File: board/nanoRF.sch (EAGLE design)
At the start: 19 parts

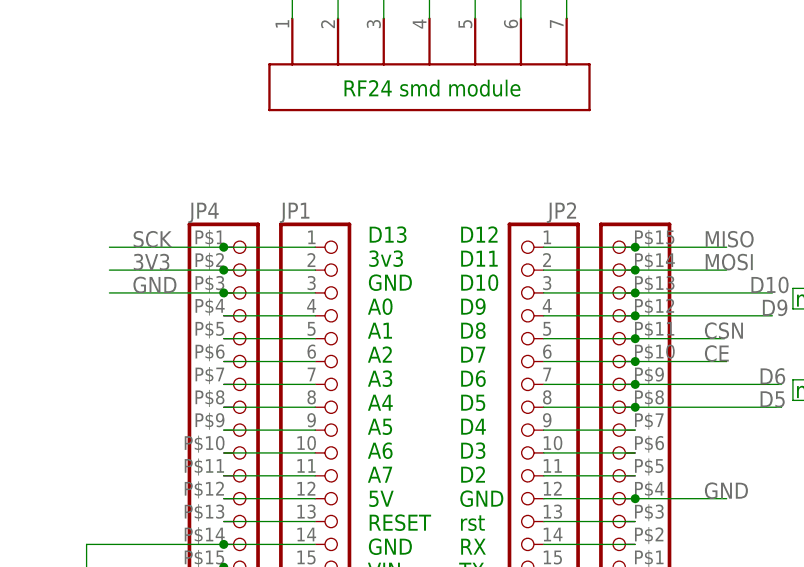
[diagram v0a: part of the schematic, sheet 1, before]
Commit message: changed prj name and files to nanoRF, starting fix for AREF pin
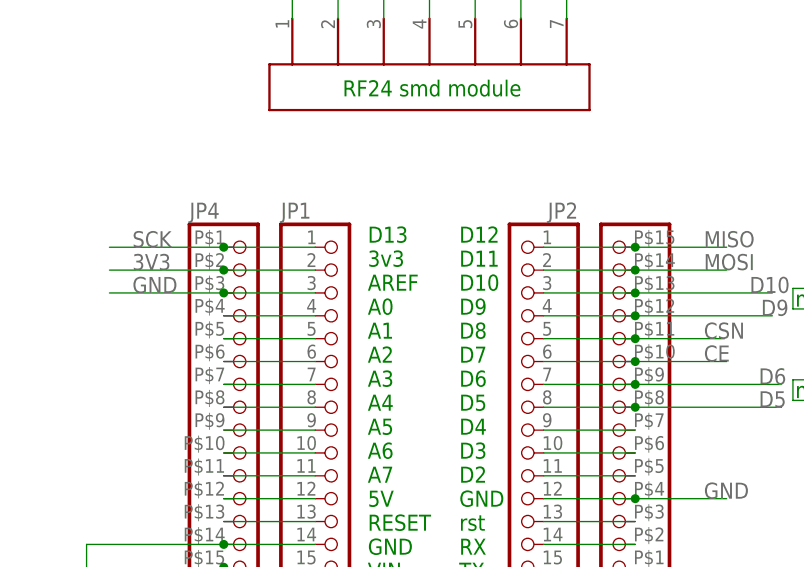
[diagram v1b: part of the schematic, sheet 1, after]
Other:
- note added: "D13 3v3 AREF A0 A1 A2 A3 A4 A5 A6 A7 5V RESET GND VIN"
- note removed: "D13 3v3 GND A0 A1 A2 A3 A4 A5 A6 A7 5V RESET GND VIN"
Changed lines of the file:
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@@
 <?xml version="1.0" encoding="utf-8"?>
 <!DOCTYPE eagle SYSTEM "eagle.dtd">
-<eagle version="8.0.0">
+<eagle version="7.6.0">
 <drawing>
 <settings>
@@
 <grid distance="0.1" unitdist="inch" unit="inch" style="lines" multiple="1" display="no" altdistance="0.01" altunitdist="inch" altunit="inch"/>
 <layers>
-<layer number="1" name="Top" color="4" fill="1" visible="yes" active="no"/>
-<layer number="2" name="Route2" color="1" fill="3" visible="yes" active="no"/>
-<layer number="3" name="Route3" color="4" fill="3" visible="yes" active="no"/>
-<layer number="4" name="Route4" color="1" fill="4" visible="yes" active="no"/>
-<layer number="5" name="Route5" color="4" fill="4" visible="yes" active="no"/>
-<layer number="6" name="Route6" color="1" fill="8" visible="yes" active="no"/>
-<layer number="7" name="Route7" color="4" fill="8" visible="yes" active="no"/>
-<layer number="8" name="Route8" color="1" fill="2" visible="yes" active="no"/>
-<layer number="9" name="Route9" color="4" fill="2" visible="yes" active="no"/>
-<layer number="10" name="Route10" color="1" fill="7" visible="yes" active="no"/>
-<layer number="11" name="Route11" color="4" fill="7" visible="yes" active="no"/>
-<layer number="12" name="Route12" color="1" fill="5" visible="yes" active="no"/>
-<layer number="13" name="Route13" color="4" fill="5" visible="yes" active="no"/>
-<layer number="14" name="Route14" color="1" fill="6" visible="yes" active="no"/>
-<layer number="15" name="Route15" color="4" fill="6" visible="yes" active="no"/>
-<layer number="16" name="Bottom" color="1" fill="1" visible="yes" active="no"/>
-<layer number="17" name="Pads" color="2" fill="1" visible="yes" active="no"/>
-<layer number="18" name="Vias" color="2" fill="1" visible="yes" active="no"/>
-<layer number="19" name="Unrouted" color="6" fill="1" visible="yes" active="no"/>
-<layer number="20" name="Dimension" color="15" fill="1" visible="yes" active="no"/>
-<layer number="21" name="tPlace" color="7" fill="1" visible="yes" active="no"/>
-<layer number="22" name="bPlace" color="7" fill="1" visible="yes" active="no"/>
-<layer number="23" name="tOrigins" color="15" fill="1" visible="yes" active="no"/>
-<layer number="24" name="bOrigins" color="15" fill="1" visible="yes" active="no"/>
-<layer number="25" name="tNames" color="7" fill="1" visible="yes" active="no"/>
-<layer number="26" name="bNames" color="7" fill="1" visible="yes" active="no"/>
-<layer number="27" name="tValues" color="7" fill="1" visible="yes" active="no"/>
-<layer number="28" name="bValues" color="7" fill="1" visible="yes" active="no"/>
+<layer number="1" name="Top" color="4" fill="1" visible="no" active="no"/>
+<layer number="2" name="Route2" color="1" fill="3" visible="no" active="no"/>
+<layer number="3" name="Route3" color="4" fill="3" visible="no" active="no"/>
+<layer number="4" name="Route4" color="1" fill="4" visible="no" active="no"/>
+<layer number="5" name="Route5" color="4" fill="4" visible="no" active="no"/>
+<layer number="6" name="Route6" color="1" fill="8" visible="no" active="no"/>
+<layer number="7" name="Route7" color="4" fill="8" visible="no" active="no"/>
+<layer number="8" name="Route8" color="1" fill="2" visible="no" active="no"/>
+<layer number="9" name="Route9" color="4" fill="2" visible="no" active="no"/>
+<layer number="10" name="Route10" color="1" fill="7" visible="no" active="no"/>
+<layer number="11" name="Route11" color="4" fill="7" visible="no" active="no"/>
+<layer number="12" name="Route12" color="1" fill="5" visible="no" active="no"/>
+<layer number="13" name="Route13" color="4" fill="5" visible="no" active="no"/>
+<layer number="14" name="Route14" color="1" fill="6" visible="no" active="no"/>
+<layer number="15" name="Route15" color="4" fill="6" visible="no" active="no"/>
+<layer number="16" name="Bottom" color="1" fill="1" visible="no" active="no"/>
+<layer number="17" name="Pads" color="2" fill="1" visible="no" active="no"/>
+<layer number="18" name="Vias" color="2" fill="1" visible="no" active="no"/>
+<layer number="19" name="Unrouted" color="6" fill="1" visible="no" active="no"/>
+<layer number="20" name="Dimension" color="15" fill="1" visible="no" active="no"/>
+<layer number="21" name="tPlace" color="7" fill="1" visible="no" active="no"/>
+<layer number="22" name="bPlace" color="7" fill="1" visible="no" active="no"/>
+<layer number="23" name="tOrigins" color="15" fill="1" visible="no" active="no"/>
+<layer number="24" name="bOrigins" color="15" fill="1" visible="no" active="no"/>
+<layer number="25" name="tNames" color="7" fill="1" visible="no" active="no"/>
+<layer number="26" name="bNames" color="7" fill="1" visible="no" active="no"/>
+<layer number="27" name="tValues" color="7" fill="1" visible="no" active="no"/>
+<layer number="28" name="bValues" color="7" fill="1" visible="no" active="no"/>
 <layer number="29" name="tStop" color="7" fill="3" visible="no" active="no"/>
 <layer number="30" name="bStop" color="7" fill="6" visible="no" active="no"/>
@@
 <layer number="35" name="tGlue" color="7" fill="4" visible="no" active="no"/>
 <layer number="36" name="bGlue" color="7" fill="5" visible="no" active="no"/>
-<layer number="37" name="tTest" color="7" fill="1" visible="yes" active="no"/>
-<layer number="38" name="bTest" color="7" fill="1" visible="yes" active="no"/>
+<layer number="37" name="tTest" color="7" fill="1" visible="no" active="no"/>
+<layer number="38" name="bTest" color="7" fill="1" visible="no" active="no"/>
 <layer number="39" name="tKeepout" color="4" fill="11" visible="no" active="no"/>
 <layer number="40" name="bKeepout" color="1" fill="11" visible="no" active="no"/>
@@
 <layer number="44" name="Drills" color="7" fill="1" visible="no" active="no"/>
 <layer number="45" name="Holes" color="7" fill="1" visible="no" active="no"/>
-<layer number="46" name="Milling" color="3" fill="1" visible="yes" active="no"/>
-<layer number="47" name="Measures" color="7" fill="1" visible="yes" active="no"/>
-<layer number="48" name="Document" color="7" fill="1" visible="yes" active="no"/>
-<layer number="49" name="Reference" color="7" fill="1" visible="yes" active="no"/>
-<layer number="50" name="dxf" color="7" fill="1" visible="yes" active="no"/>
-<layer number="51" name="tDocu" color="7" fill="1" visible="yes" active="no"/>
-<layer number="52" name="bDocu" color="7" fill="1" visible="yes" active="no"/>
-<layer number="53" name="tGND_GNDA" color="7" fill="9" visible="yes" active="no"/>
-<layer number="54" name="bGND_GNDA" color="1" fill="9" visible="yes" active="no"/>
-<layer number="56" name="wert" color="7" fill="1" visible="yes" active="no"/>
-<layer number="57" name="tCAD" color="7" fill="1" visible="yes" active="no"/>
+<layer number="46" name="Milling" color="3" fill="1" visible="no" active="no"/>
+<layer number="47" name="Measures" color="7" fill="1" visible="no" active="no"/>
+<layer number="48" name="Document" color="7" fill="1" visible="no" active="no"/>
+<layer number="49" name="Reference" color="7" fill="1" visible="no" active="no"/>
+<layer number="50" name="dxf" color="7" fill="1" visible="no" active="no"/>
+<layer number="51" name="tDocu" color="7" fill="1" visible="no" active="no"/>
+<layer number="52" name="bDocu" color="7" fill="1" visible="no" active="no"/>
+<layer number="53" name="tGND_GNDA" color="7" fill="9" visible="no" active="no"/>
+<layer number="54" name="bGND_GNDA" color="1" fill="9" visible="no" active="no"/>
+<layer number="56" name="wert" color="7" fill="1" visible="no" active="no"/>
+<layer number="57" name="tCAD" color="7" fill="1" visible="no" active="no"/>
 <layer number="90" name="Modules" color="5" fill="1" visible="yes" active="yes"/>
 <layer number="91" name="Nets" color="2" fill="1" visible="yes" active="yes"/>
@@
 <text x="49.022" y="29.21" size="1.778" layer="91">D13
 3v3
-GND
+AREF
 A0
 A1

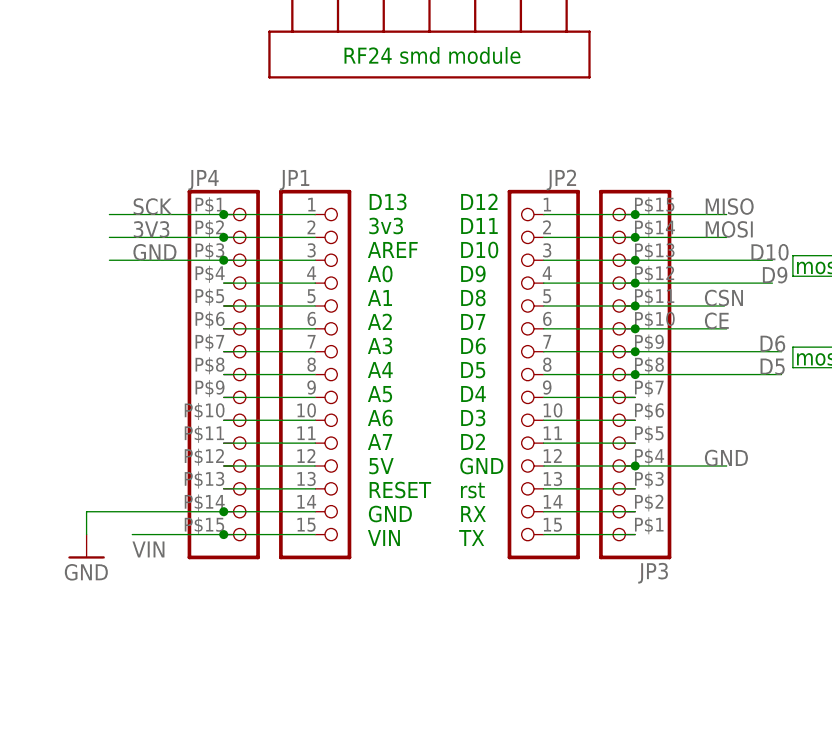
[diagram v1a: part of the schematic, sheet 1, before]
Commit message: fixed Aref pin horror
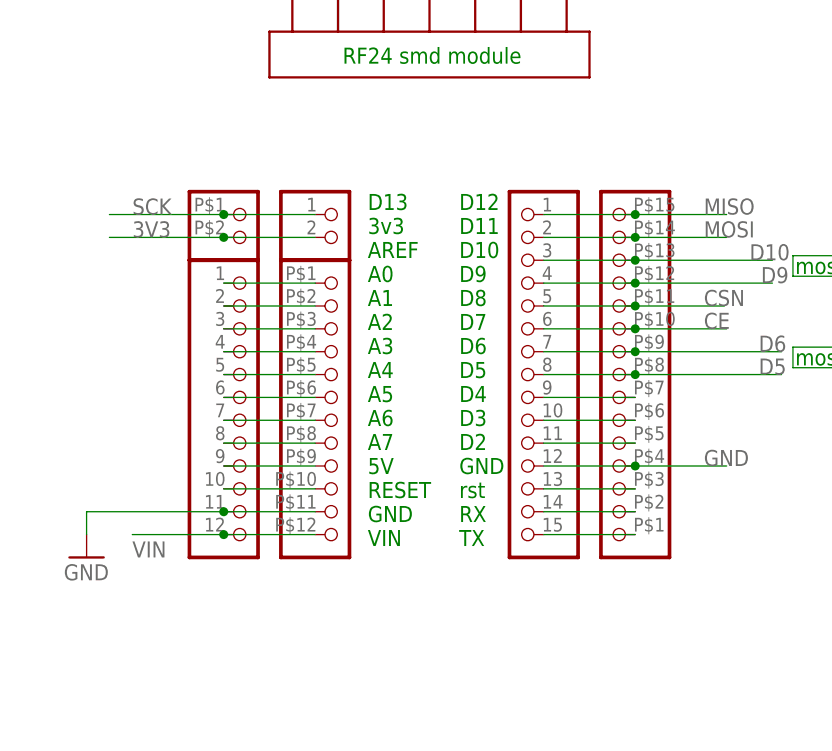
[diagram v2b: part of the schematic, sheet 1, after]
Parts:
- removed JP1: (no value), nano24rf:HEADER-1X15RND
- removed JP4: (no value), nano24rf:HEADER-1X15LONG
- added U$11: HEADER_1X2ROUND, nanoRF:HEADER_1X2ROUND
- added U$6: HEADER-1X12LONG, nanoRF:HEADER-1X12LONG
- added U$7: HEADER-1X12ROUND, nanoRF:HEADER-1X12ROUND
- added U$8: HEADER_1X2LONG, nanoRF:HEADER_1X2LONG
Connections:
- net 3V3: now also U$11.2, U$8.2; no longer JP1.2, JP4.2
- net GND: now also U$6.11, U$7.11; no longer JP1.14, JP1.3, JP4.14, JP4.3
- net N$1: now also U$6.1, U$7.1; no longer JP1.4, JP4.4
- net N$10: now also U$6.10, U$7.10; no longer JP1.13, JP4.13
- net N$2: now also U$6.2, U$7.2; no longer JP1.5, JP4.5
- net N$3: now also U$6.3, U$7.3; no longer JP1.6, JP4.6
- net N$4: now also U$6.4, U$7.4; no longer JP1.7, JP4.7
- net N$5: now also U$6.5, U$7.5; no longer JP1.8, JP4.8
- net N$6: now also U$6.6, U$7.6; no longer JP1.9, JP4.9
- net N$7: now also U$6.7, U$7.7; no longer JP1.10, JP4.10
- net N$8: now also U$6.8, U$7.8; no longer JP1.11, JP4.11
- net N$9: now also U$6.9, U$7.9; no longer JP1.12, JP4.12
- net SCK: now also U$11.1, U$8.1; no longer JP1.1, JP4.1
- net VIN: now also U$6.12, U$7.12; no longer JP1.15, JP4.15
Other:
- note added: "NANO pinout"
- note removed: "NANO"
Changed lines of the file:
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@@
 <part name="U$3" library="ATTAMI-V0.00" deviceset="GND" device=""/>
 <part name="U$5" library="ATTAMI-V0.00" deviceset="GND" device=""/>
-<part name="JP1" library="nano24rf" deviceset="HEADER-1X15" device="RND"/>
 <part name="JP2" library="nano24rf" deviceset="HEADER-1X15" device="RND"/>
 <part name="RF24" library="nano24rf" deviceset="1X7-SMDPADS" device=""/>
@@
 <part name="U$10" library="ATTAMI-V0.00" deviceset="GND" device=""/>
 <part name="JP3" library="nano24rf" deviceset="HEADER-1X15" device="LONG"/>
-<part name="JP4" library="nano24rf" deviceset="HEADER-1X15" device="LONG"/>
+<part name="U$6" library="nanoRF" deviceset="HEADER-1X12" device="LONG"/>
+<part name="U$7" library="nanoRF" deviceset="HEADER-1X12" device="ROUND"/>
+<part name="U$8" library="nanoRF" deviceset="HEADER_1X2" device="LONG"/>
+<part name="U$11" library="nanoRF" deviceset="HEADER_1X2" device="ROUND"/>
 </parts>
 <sheets>
@@
 VIN</text>
 <text x="10.16" y="0" size="1.778" layer="91">https://github.com/shenkarSElab/nano24rf</text>
-<text x="48.26" y="71.12" size="1.778" layer="98">NANO</text>
+<text x="48.26" y="71.12" size="1.778" layer="98">NANO pinout</text>
 <text x="96.52" y="49.276" size="1.778" layer="91">mosfets</text>
 <text x="96.52" y="59.436" size="1.778" layer="91">mosfets</text>
@@
 <instance part="U$3" gate="1" x="160.02" y="25.4"/>
 <instance part="U$5" gate="1" x="17.78" y="27.94"/>
-<instance part="JP1" gate="G$1" x="45.72" y="48.26"/>
-<instance part="JP2" gate="G$1" x="66.04" y="48.26" rot="MR0"/>
+<instance part="JP2" gate="G$1" x="66.04" y="48.26" smashed="yes" rot="MR0">
+<attribute name="VALUE" x="72.39" y="25.4" size="1.778" layer="96" rot="MR0"/>
+</instance>
 <instance part="RF24" gate="G$1" x="53.34" y="81.28"/>
 <instance part="Q2" gate="G$1" x="157.48" y="63.5"/>
@@
 <instance part="U$9" gate="1" x="261.62" y="53.34" rot="R270"/>
 <instance part="U$10" gate="1" x="187.96" y="55.88" rot="R270"/>
-<instance part="JP3" gate="G$1" x="76.2" y="48.26" rot="R180"/>
-<instance part="JP4" gate="G$1" x="35.56" y="48.26"/>
+<instance part="JP3" gate="G$1" x="76.2" y="48.26" smashed="yes" rot="R180">
+<attribute name="VALUE" x="82.55" y="71.12" size="1.778" layer="96" rot="R180"/>
+</instance>
+<instance part="U$6" gate="G$1" x="45.72" y="45.72" smashed="yes"/>
+<instance part="U$7" gate="G$1" x="35.56" y="45.72" smashed="yes"/>
+<instance part="U$8" gate="G$1" x="35.56" y="63.5" smashed="yes"/>
+<instance part="U$11" gate="G$1" x="45.72" y="63.5" smashed="yes"/>
 </instances>
 <busses>
@@
 </segment>
 <segment>
-<pinref part="JP1" gate="G$1" pin="14"/>
 <pinref part="U$5" gate="1" pin="GND"/>
 <wire x1="43.18" y1="33.02" x2="33.02" y2="33.02" width="0.1524" layer="91"/>
 <wire x1="33.02" y1="33.02" x2="17.78" y2="33.02" width="0.1524" layer="91"/>
 <wire x1="17.78" y1="33.02" x2="17.78" y2="30.48" width="0.1524" layer="91"/>
-<pinref part="JP4" gate="G$1" pin="14"/>
 <junction x="33.02" y="33.02"/>
+<pinref part="U$7" gate="G$1" pin="11"/>
+<pinref part="U$6" gate="G$1" pin="11"/>
 </segment>
 <segment>
@@
 <wire x1="78.74" y1="38.1" x2="88.9" y2="38.1" width="0.1524" layer="91"/>
 <junction x="78.74" y="38.1"/>
-</segment>
-<segment>
-<pinref part="JP1" gate="G$1" pin="3"/>
-<label x="22.86" y="60.96" size="1.778" layer="95"/>
-<wire x1="43.18" y1="60.96" x2="33.02" y2="60.96" width="0.1524" layer="91"/>
-<pinref part="JP4" gate="G$1" pin="3"/>
-<wire x1="33.02" y1="60.96" x2="20.32" y2="60.96" width="0.1524" layer="91"/>
-<junction x="33.02" y="60.96"/>
 </segment>
 <segment>
@@
 <net name="3V3" class="0">
 <segment>
-<pinref part="JP1" gate="G$1" pin="2"/>
 <label x="22.86" y="63.5" size="1.778" layer="95"/>
 <wire x1="43.18" y1="63.5" x2="33.02" y2="63.5" width="0.1524" layer="91"/>
-<pinref part="JP4" gate="G$1" pin="2"/>
 <wire x1="33.02" y1="63.5" x2="20.32" y2="63.5" width="0.1524" layer="91"/>
 <junction x="33.02" y="63.5"/>
+<pinref part="U$8" gate="G$1" pin="2"/>
+<pinref part="U$11" gate="G$1" pin="2"/>
 </segment>
 <segment>
@@
 <net name="VIN" class="0">
 <segment>
-<pinref part="JP1" gate="G$1" pin="15"/>
 <label x="22.86" y="27.94" size="1.778" layer="95"/>
 <wire x1="43.18" y1="30.48" x2="33.02" y2="30.48" width="0.1524" layer="91"/>
-<pinref part="JP4" gate="G$1" pin="15"/>
 <wire x1="33.02" y1="30.48" x2="22.86" y2="30.48" width="0.1524" layer="91"/>
 <junction x="33.02" y="30.48"/>
+<pinref part="U$7" gate="G$1" pin="12"/>
+<pinref part="U$6" gate="G$1" pin="12"/>
 </segment>
 <segment>
@@
 <net name="SCK" class="0">
 <segment>
-<pinref part="JP1" gate="G$1" pin="1"/>
 <wire x1="43.18" y1="66.04" x2="33.02" y2="66.04" width="0.1524" layer="91"/>
 <label x="22.86" y="66.04" size="1.778" layer="95"/>
-<pinref part="JP4" gate="G$1" pin="1"/>
 <wire x1="33.02" y1="66.04" x2="20.32" y2="66.04" width="0.1524" layer="91"/>
 <junction x="33.02" y="66.04"/>
+<pinref part="U$8" gate="G$1" pin="1"/>
+<pinref part="U$11" gate="G$1" pin="1"/>
 </segment>
 <segment>
@@
 <net name="N$1" class="0">
 <segment>
-<pinref part="JP4" gate="G$1" pin="4"/>
-<pinref part="JP1" gate="G$1" pin="4"/>
 <wire x1="33.02" y1="58.42" x2="43.18" y2="58.42" width="0.1524" layer="91"/>
+<pinref part="U$7" gate="G$1" pin="1"/>
+<pinref part="U$6" gate="G$1" pin="1"/>
 </segment>
 </net>
 <net name="N$2" class="0">
 <segment>
-<pinref part="JP1" gate="G$1" pin="5"/>
-<pinref part="JP4" gate="G$1" pin="5"/>
 <wire x1="43.18" y1="55.88" x2="33.02" y2="55.88" width="0.1524" layer="91"/>
+<pinref part="U$7" gate="G$1" pin="2"/>
+<pinref part="U$6" gate="G$1" pin="2"/>
 </segment>
 </net>
 <net name="N$3" class="0">
 <segment>
-<pinref part="JP4" gate="G$1" pin="6"/>
-<pinref part="JP1" gate="G$1" pin="6"/>
 <wire x1="33.02" y1="53.34" x2="43.18" y2="53.34" width="0.1524" layer="91"/>
+<pinref part="U$7" gate="G$1" pin="3"/>
+<pinref part="U$6" gate="G$1" pin="3"/>
 </segment>
 </net>
 <net name="N$4" class="0">
 <segment>
-<pinref part="JP1" gate="G$1" pin="7"/>
-<pinref part="JP4" gate="G$1" pin="7"/>
 <wire x1="43.18" y1="50.8" x2="33.02" y2="50.8" width="0.1524" layer="91"/>
+<pinref part="U$7" gate="G$1" pin="4"/>
+<pinref part="U$6" gate="G$1" pin="4"/>
 </segment>
 </net>
 <net name="N$5" class="0">
 <segment>
-<pinref part="JP4" gate="G$1" pin="8"/>
-<pinref part="JP1" gate="G$1" pin="8"/>
 <wire x1="33.02" y1="48.26" x2="43.18" y2="48.26" width="0.1524" layer="91"/>
+<pinref part="U$7" gate="G$1" pin="5"/>
+<pinref part="U$6" gate="G$1" pin="5"/>
 </segment>
 </net>
 <net name="N$6" class="0">
 <segment>
-<pinref part="JP1" gate="G$1" pin="9"/>
-<pinref part="JP4" gate="G$1" pin="9"/>
 <wire x1="43.18" y1="45.72" x2="33.02" y2="45.72" width="0.1524" layer="91"/>
+<pinref part="U$7" gate="G$1" pin="6"/>
+<pinref part="U$6" gate="G$1" pin="6"/>
 </segment>
 </net>
 <net name="N$7" class="0">
 <segment>
-<pinref part="JP4" gate="G$1" pin="10"/>
-<pinref part="JP1" gate="G$1" pin="10"/>
 <wire x1="33.02" y1="43.18" x2="43.18" y2="43.18" width="0.1524" layer="91"/>
+<pinref part="U$7" gate="G$1" pin="7"/>
+<pinref part="U$6" gate="G$1" pin="7"/>
 </segment>
 </net>
 <net name="N$8" class="0">
 <segment>
-<pinref part="JP1" gate="G$1" pin="11"/>
-<pinref part="JP4" gate="G$1" pin="11"/>
 <wire x1="43.18" y1="40.64" x2="33.02" y2="40.64" width="0.1524" layer="91"/>
+<pinref part="U$7" gate="G$1" pin="8"/>
+<pinref part="U$6" gate="G$1" pin="8"/>
 </segment>
 </net>
 <net name="N$9" class="0">
 <segment>
-<pinref part="JP4" gate="G$1" pin="12"/>
-<pinref part="JP1" gate="G$1" pin="12"/>
 <wire x1="33.02" y1="38.1" x2="43.18" y2="38.1" width="0.1524" layer="91"/>
+<pinref part="U$7" gate="G$1" pin="9"/>
+<pinref part="U$6" gate="G$1" pin="9"/>
 </segment>
 </net>
 <net name="N$10" class="0">
 <segment>
-<pinref part="JP1" gate="G$1" pin="13"/>
-<pinref part="JP4" gate="G$1" pin="13"/>
 <wire x1="43.18" y1="35.56" x2="33.02" y2="35.56" width="0.1524" layer="91"/>
-</segment>
-</net>
+<pinref part="U$7" gate="G$1" pin="10"/>
+<pinref part="U$6" gate="G$1" pin="10"/>
+</segment>
+</net>
